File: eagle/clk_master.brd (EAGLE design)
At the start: 76.2 x 50.8 mm, 68 parts, among them U1 74LVCU04A, U2 MCP1824ST-3302E, U3 ATXMEGA16A4U, U4 ENC28J60, U5 TESEO-LIV3R, U8 74LVC74A, U9 74LVC86A

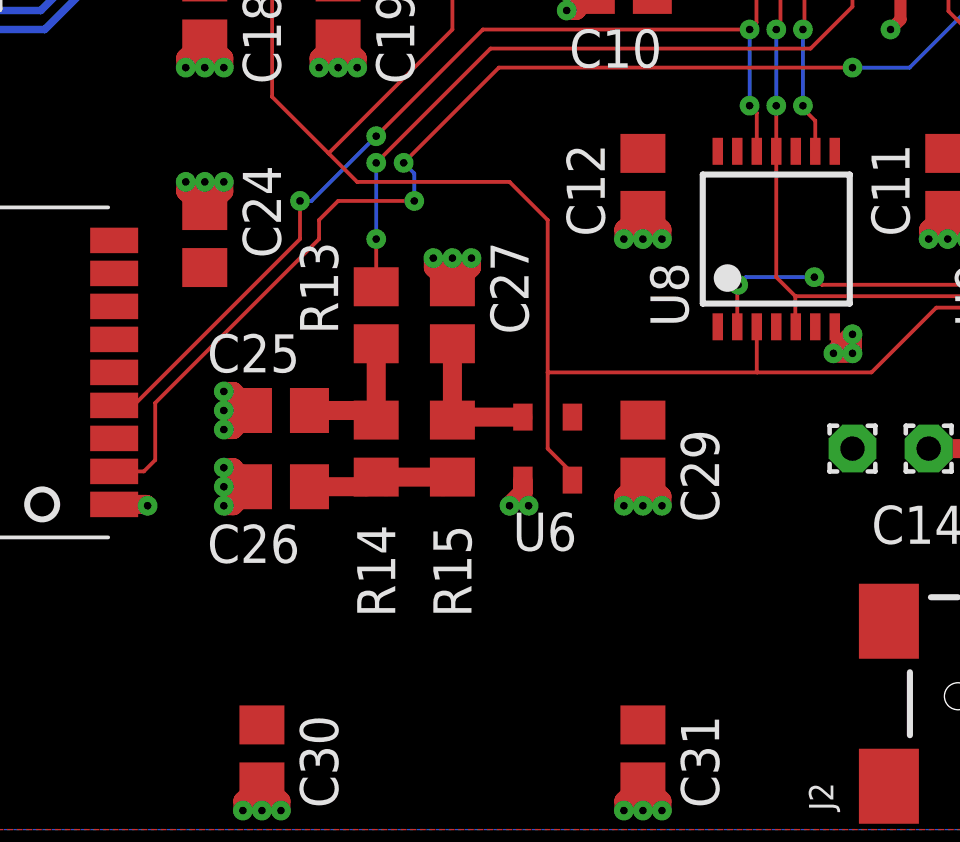
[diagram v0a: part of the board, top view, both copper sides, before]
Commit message: change master clock oscillator footprint
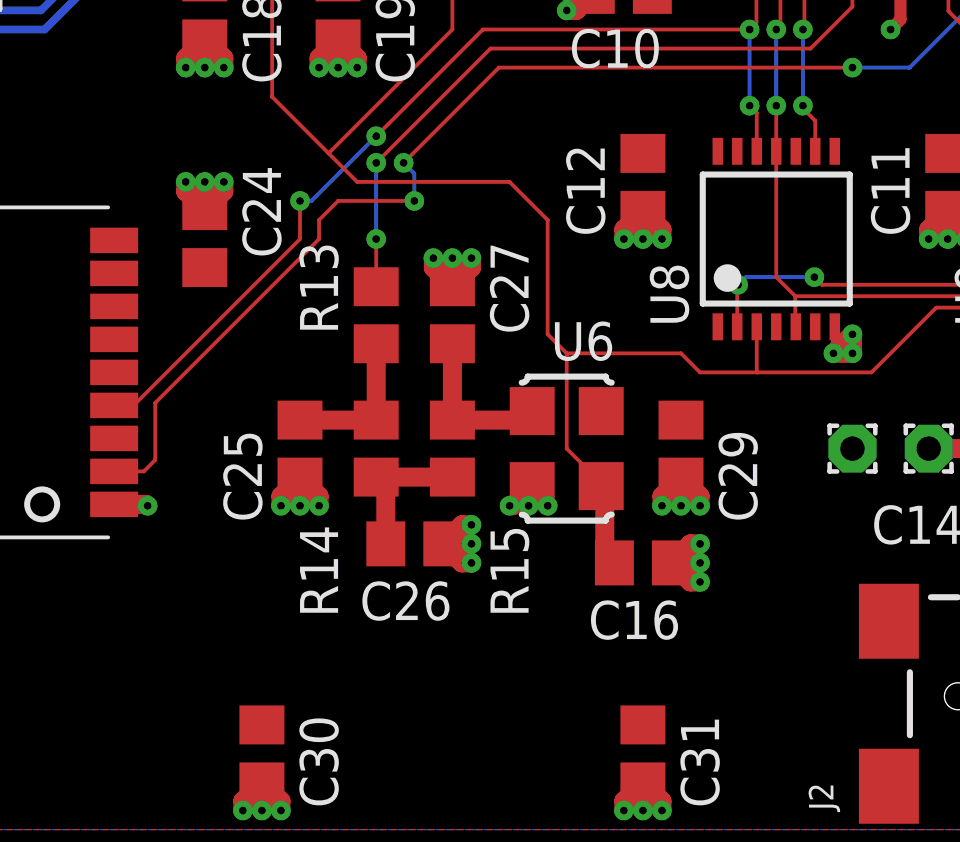
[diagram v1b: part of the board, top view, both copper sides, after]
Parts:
- added C16: unpopulated, rcl:R0805
- C26: value 100u -> 3.3u
- C27: value 100n -> 100u
- R13: value 330 -> 1k
- R14: value 10k -> 3.3k
- R15: value 330 -> 10k
- U6: device crystal:ASE -> crystal:ASF
- moved C26 4.84 mm to (29.8, 10.2), turned to 0 degrees
- moved C25 1.42 mm to (26.0, 13.3), turned to 270 degrees
- moved C29 1.27 mm to (38.7, 13.3)
- moved U6 0.63 mm to (34.9, 13.3)
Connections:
- removed net FILT0: C25.1, R13.1, R14.2
- new net FILT2: C26.1, R14.1, R15.1
- net CLK_25MHZ: now also C16.1
- net FILT1: now also C25.1, R13.1, R14.2; no longer C26.1, R14.1, R15.1
- net GND: now also C16.2
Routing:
- net FILT2: track 0.00 -> 5.35 mm
- net FILT0: track 4.90 -> 0.00 mm
- net GND: track 116.0 -> 120.4 mm, vias 206 -> 210
- net CLK_25MHZ: track 70.1 -> 73.0 mm
- net FILT: track 4.94 -> 5.47 mm
